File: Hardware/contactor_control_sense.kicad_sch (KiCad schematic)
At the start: 69 parts, among them J10 ContactorConnector, J11 ContactorConnector, J15 Conn_01x02, J4 ContactorConnector, J9 ContactorConnector, Q10 PMV213SN,215, Q4 PMV213SN,215, Q5 PMV213SN,215, Q6 PMV213SN,215, Q7 PMV213SN,215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

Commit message: added BOM
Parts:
- C14, C15, C17, C22: Manufactuerer (none) -> TAIYO YUDEN; P/N C0805C105K5PACTU -> MLASU168SB5105KTNA01
- D5, D6, D8, D9: Manufactuerer (none) -> Vishay General Semiconductor; P/N (none) -> VSSAF522-M3/H
- HV+1, HV+2, HV+3, HV+4: Manufactuerer (none) -> NATIONSTAR; P/N (none) -> NCD0603R1
- J10, J11, J4, J9: Manufactuerer (none) -> Molex; P/N (none) -> 105309-1204
- J15: Manufactuerer (none) -> Molex; P/N (none) -> 105309-1102
- Q10, Q4, Q5, Q6, Q7, Q8, Q9: Manufactuerer (none) -> Nexperia; P/N (none) -> PMV213SN,215
- R19, R29, R30, R34, R38, R39, R43, R44, R45, R50, R54: Manufactuerer (none) -> Vishay; P/N (none) -> CRCW060310K0FKEI
- R20, R33, R37, R41: Manufactuerer (none) -> Vishay; P/N (none) -> CRCW06031K00FKEI
- R21, R32, R36, R40: Manufactuerer (none) -> Vishay; P/N (none) -> CRCW06034K30FKEA
- TP10, TP34, TP36, TP37, TP38, TP39, TP40, TP41, TP42, TP44, TP45, TP5, TP6, TP7, TP9: now left out of the parts list
- U4, U5, U6, U7: Manufactuerer (none) -> Everlight

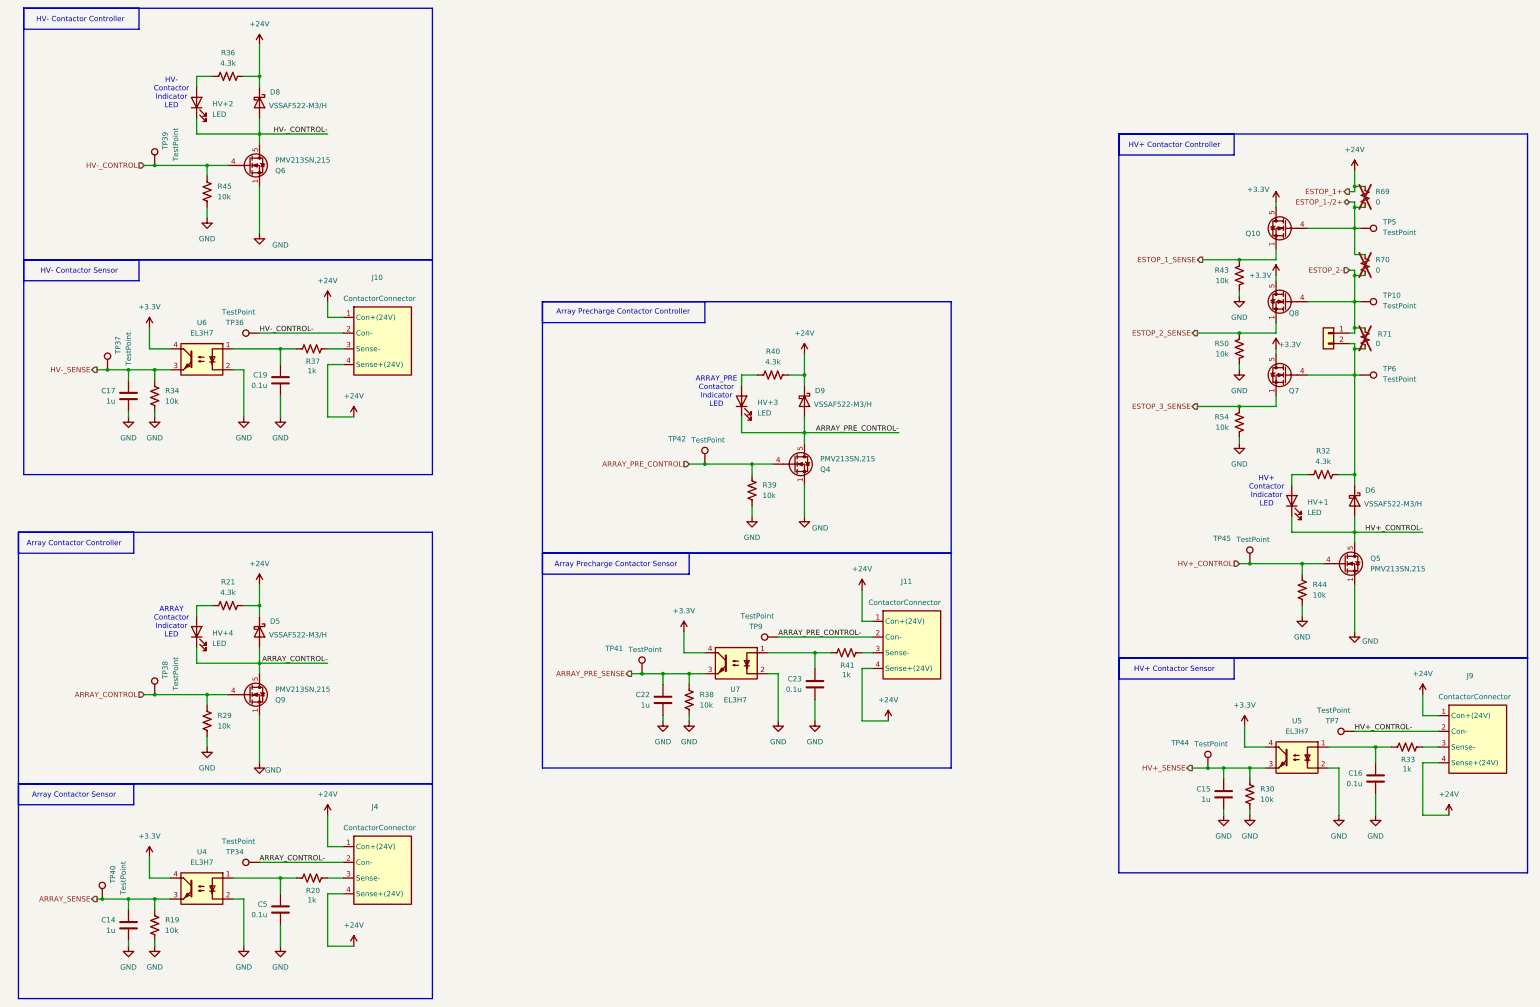
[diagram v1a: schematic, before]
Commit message: RevB PR (#14)
* RevB Schematic Update

* RevB Schematic revisions

* revB updates

* Schematic polishes, layout WIP

* circuit blocks designed, schematic updated

* unblocked SD card holder

* halfway laid-out

* unblocked SD card again

* small schematic changes

* intial layout design

* Updated LSOM footprint

* filled in copper holes. Name/REV/Date added

* RevB layout completed

* JLC Production Files

* added resistors

* replace silkscreen

* condensed custom lirbraries

* removed all unnessasary files and some nessasary ones
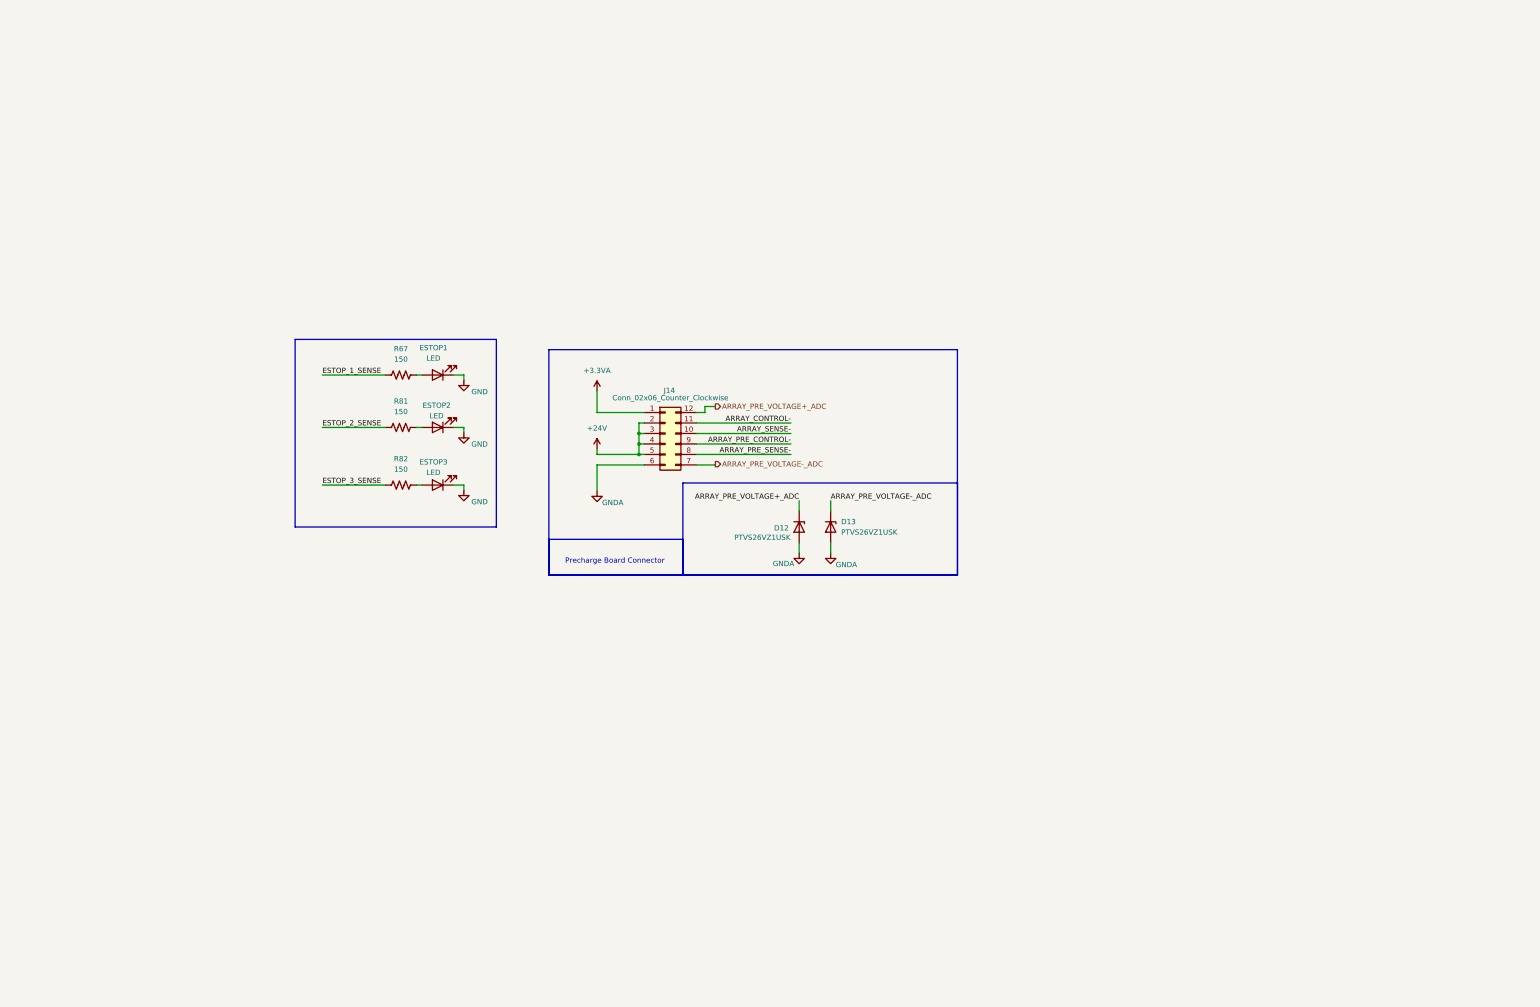
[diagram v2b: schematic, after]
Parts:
- removed C14, C15, C17, C22: 1u, Capacitor_SMD:C_0603_1608Metric, symbol Device:C
- removed C16, C19, C23, C5: 0.1u, Capacitor_SMD:C_0603_1608Metric, symbol Device:C
- removed D5, D6, D8, D9: VSSAF522-M3/H, UTSVT_Passives:MMDL101T1G, symbol Diode:C3D25170H
- removed HV+1, HV+2, HV+3, HV+4: LED, LED_SMD:LED_0603_1608Metric, symbol Device:LED
- removed J10, J11, J4, J9: ContactorConnector, UTSVT_Connectors:Molex_Nano-Fit_105309-xx04_1x04_P2.50mm_Vertical, symbol UTSVT_Connectors:ContactorConnector
- removed J15: Conn_01x02, UTSVT_Connectors:Molex_Nano-Fit_105309-xx02_1x02_P2.50mm_Vertical, symbol Connector_Generic:Conn_01x02
- removed Q10, Q4, Q5, Q6, Q7, Q8, Q9: PMV213SN,215, Package_TO_SOT_SMD:SOT-23-3, symbol Transistor_FET:BUK7M27-80EX
- removed R19, R29, R30, R34, R38, R39, R43, R44, R45, R50, R54: 10k, Resistor_SMD:R_0603_1608Metric, symbol Device:R_US
- removed R20, R33, R37, R41: 1k, Resistor_SMD:R_0603_1608Metric, symbol Device:R_US
- removed R21, R32, R36, R40: 4.3k, Resistor_SMD:R_0603_1608Metric, symbol Device:R_US
- removed R69, R70, R71: 0, Resistor_SMD:R_0603_1608Metric, symbol Device:R_Small_US
- removed TP10, TP34, TP36, TP37, TP38, TP39, TP40, TP41, TP42, TP44, TP45, TP5, TP6, TP7, TP9: TestPoint, TestPoint:TestPoint_Pad_1.0x1.0mm, symbol Connector:TestPoint
- removed U4, U5, U6, U7: EL3H7, UTSVT_ICs:EL3H7, symbol UTSVT_ICs:EL3H7
- added D12, D13: PTVS26VZ1USK, Diode_SMD:Nexperia_DSN1608-2_1.6x0.8mm, symbol Diode:PTVS26VZ1USK
- added ESTOP1, ESTOP2, ESTOP3: LED, LED_SMD:LED_0603_1608Metric, symbol Device:LED
- added J14: Conn_02x06_Counter_Clockwise, Connector_Molex:Molex_Nano-Fit_105310-xx12_2x06_P2.50mm_Vertical, symbol Connector_Generic:Conn_02x06_Counter_Clockwise
- added R67, R81, R82: 150, Resistor_SMD:R_0603_1608Metric, symbol Device:R_US
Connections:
- net +24V: now also J14.2 (Pin_2), J14.3 (Pin_3), J14.4 (Pin_4), J14.5 (Pin_5)
- net ARRAY_CONTROL-: now also J14.11 (Pin_11)
- net ARRAY_PRE_CONTROL-: now also J14.9 (Pin_9)
- net ESTOP_1_SENSE: now also R67.1
- net ESTOP_2_SENSE: now also R81.1
- net ESTOP_3_SENSE: now also R82.1
- net GND: now also ESTOP1.1 (K), ESTOP2.1 (K), ESTOP3.1 (K)
- new net: ESTOP2.2 (A), R81.2
- new net: ESTOP3.2 (A), R82.2
- new net: ESTOP1.2 (A), R67.2
- new net +3.3VA: J14.1 (Pin_1)
- new net ARRAY_PRE_SENSE-: J14.8 (Pin_8)
- new net ARRAY_PRE_VOLTAGE+_ADC: D12.1 (K), J14.12 (Pin_12)
- new net ARRAY_PRE_VOLTAGE-_ADC: D13.1 (K), J14.7 (Pin_7)
- new net ARRAY_SENSE-: J14.10 (Pin_10)
- new net GNDA: D12.2 (A), D13.2 (A), J14.6 (Pin_6)
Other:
- note added: "Precharge Board Connector"
- note removed: "ARRAY Contactor Indicator LED"
- note removed: "ARRAY_PRE Contactor Indicator LED"
- note removed: "Array Contactor Controller"
- note removed: "Array Contactor Sensor"
- note removed: "Array Precharge Contactor Controller"
- note removed: "Array Precharge Contactor Sensor"
- note removed: "HV+ Contactor Controller"
- note removed: "HV+ Contactor Indicator LED"
- note removed: "HV+ Contactor Sensor"
- note removed: "HV- Contactor Controller"
- note removed: "HV- Contactor Indicator LED"
- note removed: "HV- Contactor Sensor"
